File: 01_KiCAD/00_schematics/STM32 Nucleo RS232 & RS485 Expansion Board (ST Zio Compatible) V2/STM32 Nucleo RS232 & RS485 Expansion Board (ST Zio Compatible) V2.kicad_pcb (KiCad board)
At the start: 4 copper layers, 72 x 133.4 mm, 182 parts, among them CN10 Conn_02x17_Odd_Even, CN7 Conn_02x10_Odd_Even, CN8 Conn_02x08_Odd_Even, CN9 Conn_02x15_Odd_Even, IC1 REG103GA-A, J1 1190299, J10 DIR, J11 TERM_TX, J12 TERM_RX, J13 SLR, J14 HD-A(Y), J15 HD-B(Z), J2 CONN D-SUB PLUG 9POS TH, J3 TCVR_PWR, J4 TX_LED, J5 RX_LED, J6 SW_ENA, J7 MODE0, J8 MODE1, J9 MODE2, U1 TPS2117DRLR, U11 SN74LVC2G14DBV, U12 SN74LVC14ADR, U2 THVD4431RHAR, U3 SN74LVC2G14DBV, U4 SN74LVC245ADBR, U5 SN74LVC14ADR, U6 NUCLEO-H753ZI

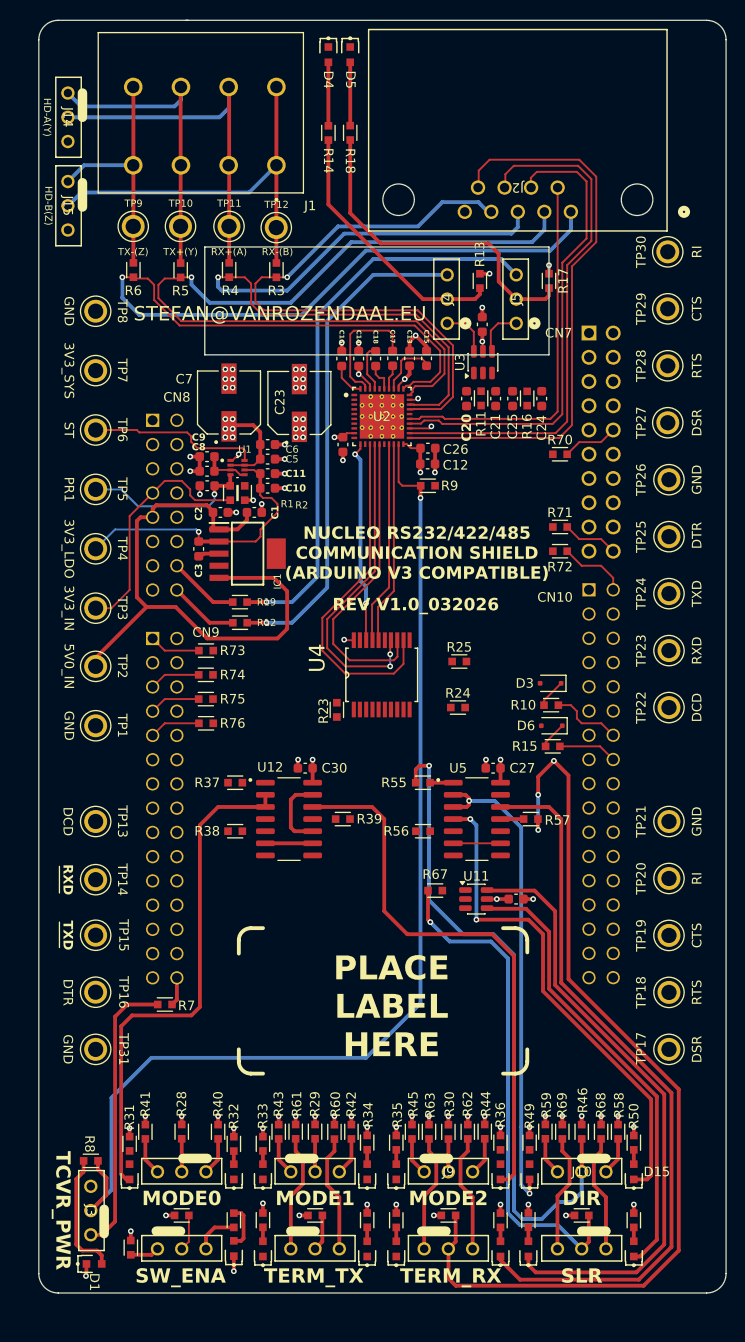
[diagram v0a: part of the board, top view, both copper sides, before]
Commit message: Finalizing roting
Made some final routings and updated Netlist name on the schematics for some of the RS232 testpoints.
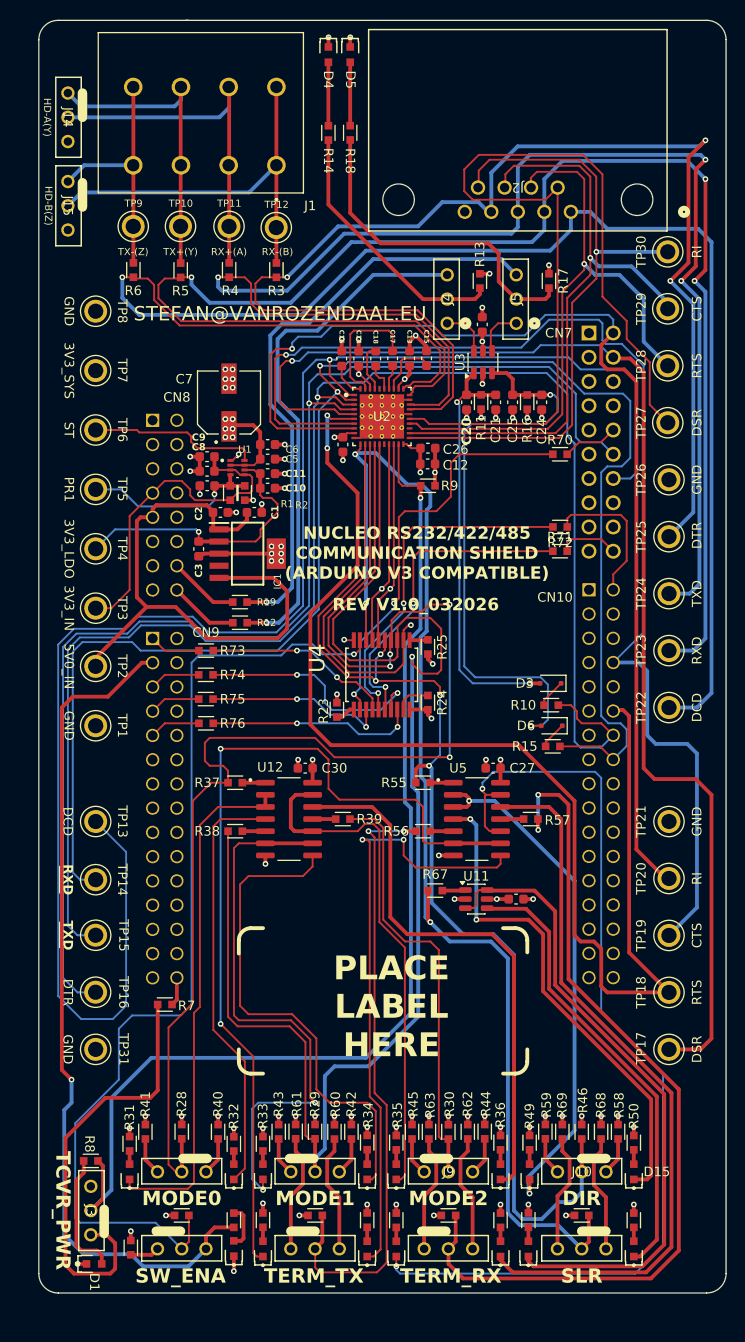
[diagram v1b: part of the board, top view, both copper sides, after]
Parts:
- removed C23: 47µF, EEEFT1H470AP:CAP_EEEFT1H470AP
- moved R25 3.63 mm to (68.6, 102.5), turned to -90 degrees
- moved R24 3.19 mm to (68.6, 108.3), turned to -90 degrees
- moved R72 2.54 mm to (82.4, 89.9)
- moved R71 2.54 mm to (82.4, 92.5)
- moved C20 0.38 mm to (72.6, 76.8)
- moved C21 0.38 mm to (75.7, 76.8)
- moved C24 0.38 mm to (80.5, 76.8)
- moved C25 0.38 mm to (77.5, 76.8)
- moved R11 0.38 mm to (74.2, 76.8)
- moved R16 0.38 mm to (79.0, 76.8)
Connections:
- TP27 pad TP: /RS232 & RS485 Tranceiver/DSR -> /RS232 & RS485 Tranceiver/DSRBus
- TP28 pad TP: /RS232 & RS485 Tranceiver/RTS -> /RS232 & RS485 Tranceiver/RTSBus
- TP29 pad TP: /RS232 & RS485 Tranceiver/CTS -> /RS232 & RS485 Tranceiver/CTSBus
- TP30 pad TP: /RS232 & RS485 Tranceiver/RI -> /RS232 & RS485 Tranceiver/RIBus
- U2 pad 42: (no net) -> GND
- U2 pad 43: (no net) -> GND
- U2 pad 44: (no net) -> GND
- U2 pad 45: (no net) -> GND
- U2 pad 46: (no net) -> GND
- U2 pad 47: (no net) -> GND
- U2 pad 48: (no net) -> GND
- U2 pad 49: (no net) -> GND
- U2 pad 50: (no net) -> GND
- U2 pad 51: (no net) -> GND
- U2 pad 52: (no net) -> GND
- U2 pad 53: (no net) -> GND
- U2 pad 54: (no net) -> GND
- U2 pad 55: (no net) -> GND
- U2 pad 56: (no net) -> GND
- U2 pad 57: (no net) -> GND
- U2 pad 58: (no net) -> GND
- U2 pad 59: (no net) -> GND
- U2 pad 60: (no net) -> GND
- U2 pad 61: (no net) -> GND
- U2 pad 62: (no net) -> GND
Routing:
- net L1-DCD: track 0.00 -> 173.1 mm, vias 0 -> 1
- net L2-RXD: track 6.16 -> 166.1 mm, vias 0 -> 2
- net L3-TXD: track 7.50 -> 165.3 mm, vias 0 -> 1
- net L4-DTR: track 0.00 -> 135.0 mm, vias 0 -> 1
- net L5-DSR: track 0.00 -> 132.4 mm, vias 0 -> 1
- net L6-RTS: track 0.00 -> 131.2 mm, vias 0 -> 2
- net L7-CTS: track 0.00 -> 127.5 mm, vias 0 -> 1
- net L8-RI: track 0.00 -> 118.6 mm, vias 0 -> 1
- net MODE1: track 35.7 -> 151.7 mm, vias 0 -> 1
- net MODE2: track 39.5 -> 145.1 mm, vias 0 -> 1
- net Net-(D18-K): track 0.00 -> 103.8 mm, vias 0 -> 2
- net MODE0: track 37.1 -> 139.7 mm, vias 2 -> 4
- net Net-(J6-Pin_2): track 3.82 -> 102.6 mm, vias 0 -> 1
- net TERM_TX: track 25.5 -> 120.1 mm, vias 0 -> 3
- net Net-(D16-K): track 4.95 -> 97.7 mm, vias 0 -> 2
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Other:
- outline, holes or cut-outs redrawn

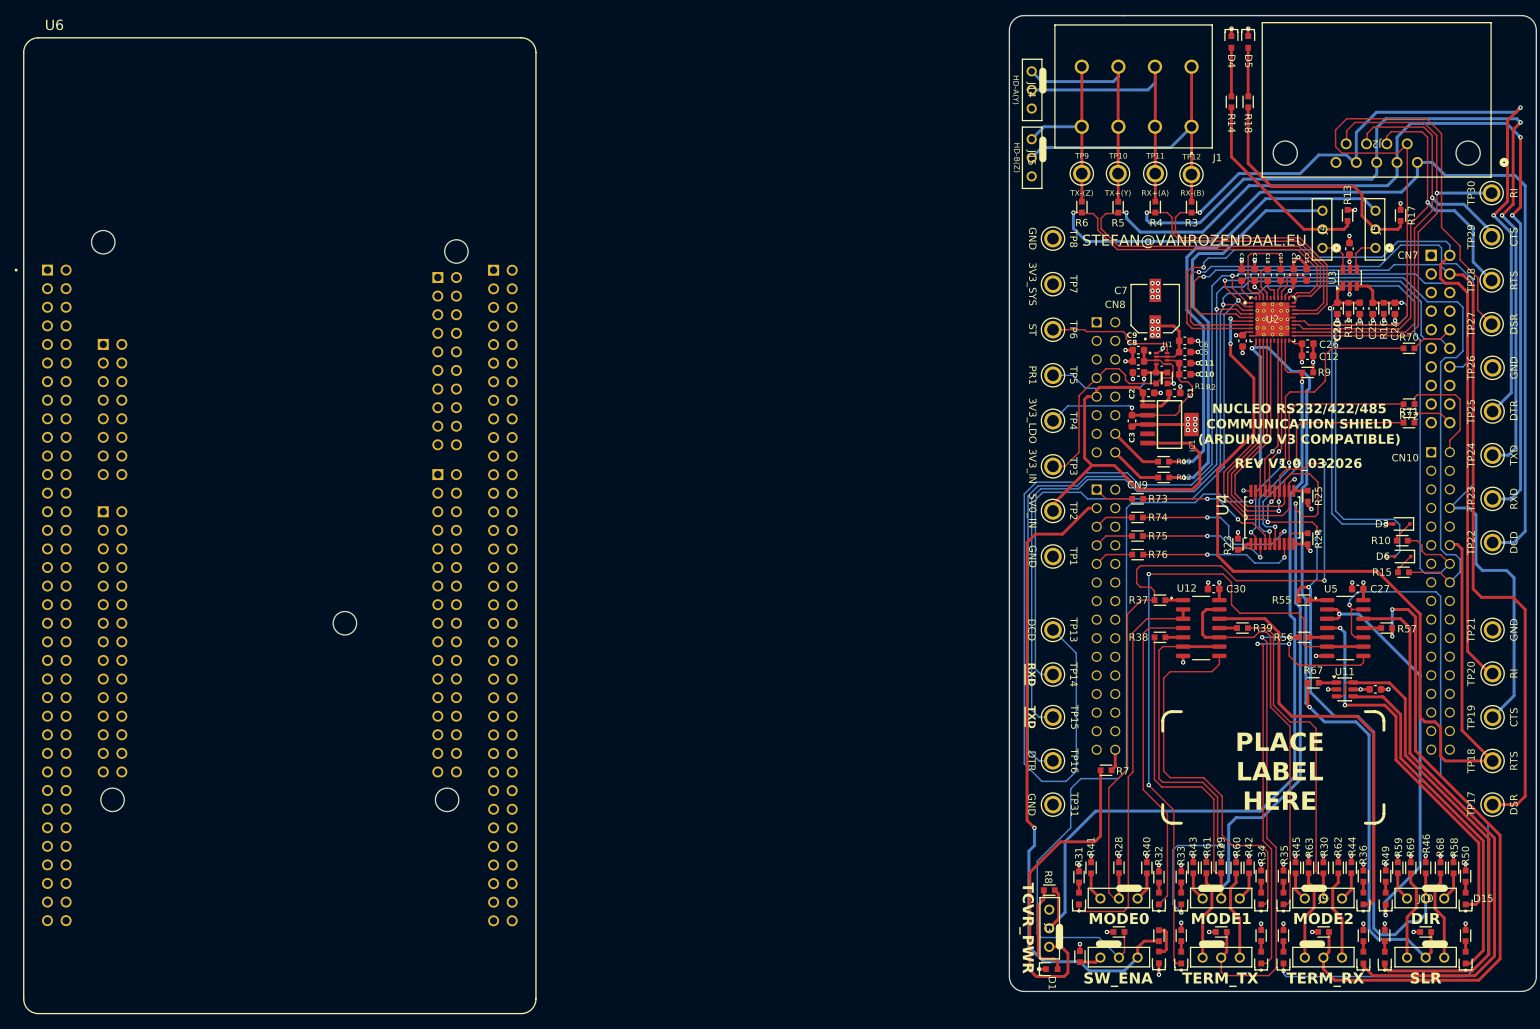
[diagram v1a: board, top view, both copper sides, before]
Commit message: Finalizing PCB Design
Finalizing track routing on PCB and run DRC. Made some minor silkscreen adjustments.
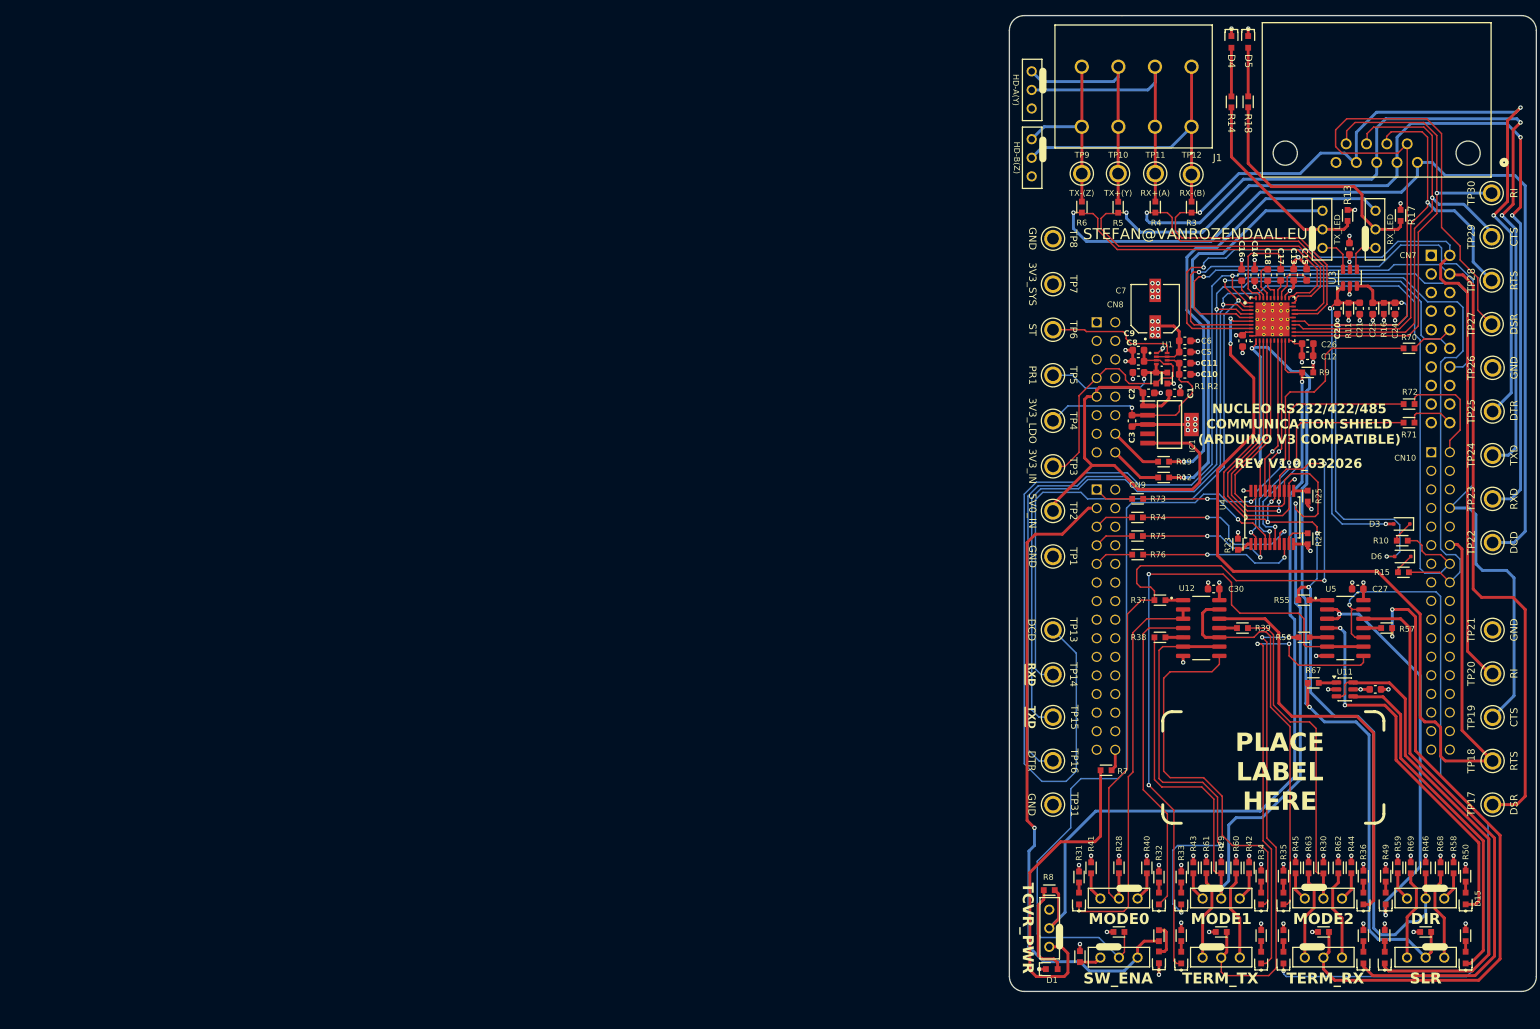
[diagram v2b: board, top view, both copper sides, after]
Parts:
- removed U6: NUCLEO-H753ZI, NUCLEO-H753ZI:MODULE_NUCLEO-H753ZI
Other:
- outline, holes or cut-outs redrawn
- rule pad_to_mask_clearance: 0.05 -> -0.05
- board text added: "≥8 MIL VIAS REQUIRE CONDUCTIVE FILL AND PLANARIZE"
- board text removed: "XX MIL VIAS REQUIRE CONDUCTIVE FILL AND PLANARIZE"

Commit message: Complete redesign
Redesigned the complete board. Added hardware termination jumpers for 1120R resistors for RS485. Changes footprint, package size and simplified values between capacitors.
Still need to re-route the entire board :-(
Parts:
- removed C33: 100nF, PCM_SparkFun-Capacitor:C_0603_1608Metric
- removed D21: LED, IN-S63AT:LED_0603_WRE
- removed IC1: REG103GA-A, REG103GA-A:SOT127P706X180-6N
- removed U11: SN74LVC2G14DBV, Package_TO_SOT_SMD:SOT-23-6
- removed U12: SN74LVC14ADR, SN74LVC14ADR:SOIC127P600X175-14N
- added C23: 470nF, PCM_SparkFun-Capacitor:C_0603_1608Metric, F.Cu at (-122.9, 80.4)
- added C28: 100nF, PCM_SparkFun-Capacitor:C_0603_1608Metric, F.Cu at (-123.1, 71.3)
- added C29: 100nF, PCM_SparkFun-Capacitor:C_0603_1608Metric, F.Cu at (-138.1, 44.4)
- added C31: 100nF, PCM_SparkFun-Capacitor:C_0603_1608Metric, F.Cu at (-20.8, 93.9)
- added D2: BAT54J, Diode_SMD:D_SOD-323F, F.Cu at (-20.2, 88.3)
- added J16: TERM_RX, Samtec_Connector:Samtec HTSW-103-07-F-S, F.Cu at (-144.9, 41.2)
- added J17: SLR, Samtec_Connector:Samtec HTSW-103-07-F-S, F.Cu at (-144.9, 47.6)
- added R20: 137R, PCM_fab:R_0603, F.Cu at (56.1, 39.7)
- added R21: 330R, PCM_fab:R_0603, F.Cu at (-138.2, 41.8)
- added U6: SN74LVC14ADR, SN74LVC14ADR:SOIC127P600X175-14N, F.Cu at (-116.4, 72.4)
- added U7: SN74LVC14ADR, SN74LVC14ADR:SOIC127P600X175-14N, F.Cu at (-8.72, 125.3)
- added U8: SN74LVC2G14DBV, Package_TO_SOT_SMD:SOT-23-6, F.Cu at (-120.8, 101.8)
- C1, C18, C19, C2, C21, C5: footprint PCM_SparkFun-Capacitor:C_0603_1608Metric -> Capacitor_SMD:C_0805_2012Metric
- C10: value 1µF -> 2µ2; footprint PCM_SparkFun-Capacitor:C_0603_1608Metric -> Capacitor_SMD:C_1210_3225Metric
- C11: value 100nF -> 47µF; footprint PCM_SparkFun-Capacitor:C_0603_1608Metric -> EEEFT1H470AP:CAP_EEEFT1H470AP
- C12: value 1µF -> 47µF; footprint PCM_SparkFun-Capacitor:C_0603_1608Metric -> EEEFT1H470AP:CAP_EEEFT1H470AP
- C13, C14: value 1µF -> 100nF
- C15, C16, C17: value 100nF -> 1µF; footprint PCM_SparkFun-Capacitor:C_0603_1608Metric -> Capacitor_SMD:C_1206_3216Metric
- C20: value 470nF -> 100nF; footprint PCM_SparkFun-Capacitor:C_0603_1608Metric -> Capacitor_SMD:C_0805_2012Metric
- C24: value 470nF -> 100nF
- C26: value 100nF -> 470nF
- C3: value 100nF -> 2µ2; footprint PCM_SparkFun-Capacitor:C_0603_1608Metric -> Capacitor_SMD:C_0805_2012Metric
- C4: value 10nF -> 1µ; footprint PCM_SparkFun-Capacitor:C_0603_1608Metric -> Capacitor_SMD:C_0805_2012Metric
- C6: value 470nF -> 1µ; footprint PCM_SparkFun-Capacitor:C_0603_1608Metric -> Capacitor_SMD:C_0805_2012Metric
- C7: value 47µF -> 100nF; footprint EEEFT1H470AP:CAP_EEEFT1H470AP -> Capacitor_SMD:C_0805_2012Metric
- C8: value 1µF -> 100nF; footprint PCM_SparkFun-Capacitor:C_0603_1608Metric -> Capacitor_SMD:C_0603_1608Metric
- C9: value 100nF -> 1µ; footprint PCM_SparkFun-Capacitor:C_0603_1608Metric -> Capacitor_SMD:C_0805_2012Metric
- D3, D6: value BAT54J -> LED; footprint Diode_SMD:D_SOD-323F -> IN-S63AT:LED_0603_WRE
- D5: value LED -> BAT54J; footprint IN-S63AT:LED_0603_WRE -> Diode_SMD:D_SOD-323F
- J1: value 1190299 -> HD-A(Y); footprint PH1190299:PHOENIX_1190299 -> Samtec_Connector:Samtec HTSW-103-07-F-S
- J10: value DIR -> SW_ENA
- J11: value TERM_TX -> MODE0
- J12: value TERM_RX -> MODE1
- J13: value SLR -> MODE2
- J14: value HD-A(Y) -> DIR
- J15: value HD-B(Z) -> TERM_TX
- J2: value CONN D-SUB PLUG 9POS TH -> HD-B(Z); footprint SubD-M-2301843-2:CONN9_2301843-2_TEC -> Samtec_Connector:Samtec HTSW-103-07-F-S
- J3: value TCVR_PWR -> TERM_RX (A/B)
- J4: value TX_LED -> TERM_TX (Y/Z)
- J5: value RX_LED -> 1190299; footprint Samtec_Connector:Samtec HTSW-103-07-F-S -> PH1190299:PHOENIX_1190299
- J6: value SW_ENA -> CONN D-SUB PLUG 9POS TH; footprint Samtec_Connector:Samtec HTSW-103-07-F-S -> SubD-M-2301843-2:CONN9_2301843-2_TEC
- J7: value MODE0 -> TCVR_PWR
- J8: value MODE1 -> TX_LED
- J9: value MODE2 -> RX_LED
- R10: value 1K -> 590R
- R11: value 453K -> 10K
- R12: value 330R -> 1K
- R13: value 1M -> 453K
- R14: value 590R -> 330R
- R15: value 1K -> 1M
- R16: value 453K -> 590R
- R17: value 1M -> 1K
- R18: value 137R -> 453K
- R19: value 330R -> 1M
- R3, R4: value 0R -> 120R
- R7: value 330R -> 0R
- R8: value 590R -> 0R
- R9: value 10K -> 330R
- TP10: value TX+(Y) -> DCD
- TP11: value RX+(A) -> TX-(Z); footprint 5008_Orange:KEYSTONE_5008 -> 5009_Yellow:KEYSTONE_5009
- TP12: value RX-(B) -> RXD; footprint 5008_Orange:KEYSTONE_5008 -> 5009_Yellow:KEYSTONE_5009
- TP13: value DCD -> RXD
- TP14: value RXD -> TX+(Y)
- TP16: value DTR -> TXD; footprint 5009_Yellow:KEYSTONE_5009 -> 5008_Orange:KEYSTONE_5008
- TP17: value DSR -> RX+(A); footprint 5009_Yellow:KEYSTONE_5009 -> 5008_Orange:KEYSTONE_5008
- TP18: value RTS -> DTR
- TP19: value CTS -> DTR; footprint 5009_Yellow:KEYSTONE_5009 -> 5008_Orange:KEYSTONE_5008
- TP20: value RI -> RX-(B); footprint 5009_Yellow:KEYSTONE_5009 -> 5008_Orange:KEYSTONE_5008
- TP21: value GND -> DSR; footprint 5006_Black:KEYSTONE_5006 -> 5009_Yellow:KEYSTONE_5009
- TP22: value DCD -> GND; footprint 5009_Yellow:KEYSTONE_5009 -> 5006_Black:KEYSTONE_5006
- TP23: value RXD -> RTS
- TP24: value TXD -> DSR
- TP25: value DTR -> CTS; footprint 5008_Orange:KEYSTONE_5008 -> 5009_Yellow:KEYSTONE_5009
- TP26: value GND -> RTS; footprint 5006_Black:KEYSTONE_5006 -> 5008_Orange:KEYSTONE_5008
- TP27: value DSR -> RI; footprint 5008_Orange:KEYSTONE_5008 -> 5009_Yellow:KEYSTONE_5009
- TP28: value RTS -> CTS
- TP29: value CTS -> GND; footprint 5008_Orange:KEYSTONE_5008 -> 5006_Black:KEYSTONE_5006
- TP3: value 3V3_IN -> 3V3_LDO
- TP4: value 3V3_LDO -> GND; footprint 5005_Red:KEYSTONE_5005 -> 5006_Black:KEYSTONE_5006
- TP5: value PR1 -> 3V3_IN
- TP6: value ST -> 3V3_SYS; footprint 5007_White:KEYSTONE_5007 -> 5005_Red:KEYSTONE_5005
- TP7: value 3V3_SYS -> PR1
- TP8: value GND -> ST; footprint 5006_Black:KEYSTONE_5006 -> 5005_Red:KEYSTONE_5005
- TP9: value TX-(Z) -> DCD
- U1: value TPS2117DRLR -> TLV77518PDBVR; footprint TPS2117DRLR:SOTFL50P160X60-8N -> TLV77518PDBVR:SOT-23-5_1P75X3P05_TEX
- U2: value THVD4431RHAR -> TPS2117DRLR; footprint THVD4431RHAR:RHA0040R-MFG -> TPS2117DRLR:SOTFL50P160X60-8N
- U3: value SN74LVC2G14DBV -> THVD4431RHAR; footprint Package_TO_SOT_SMD:SOT-23-6 -> THVD4431RHAR:RHA0040R-MFG
- U4: value SN74LVC245ADBR -> SN74LVC2G14DBV; footprint SN74LVC245ADBR:SOP65P780X200-20N -> Package_TO_SOT_SMD:SOT-23-6
- U5: value SN74LVC14ADR -> SN74LVC245ADBR; footprint SN74LVC14ADR:SOIC127P600X175-14N -> SN74LVC245ADBR:SOP65P780X200-20N
- moved U5 214.9 mm to (-139.8, 96.0), turned to 90 degrees
- moved C30 205.5 mm to (-138.1, 46.9), turned to 0 degrees
- moved R1 185.0 mm to (-135.9, 64.5)
- moved R19 166.6 mm to (-117.1, 83.6)
- moved R12 166.3 mm to (-116.8, 86.9)
- moved R2 162.4 mm to (-111.9, 67.4)
- moved J15 147.9 mm to (-115.3, 34.0)
- moved C22 138.6 mm to (-63.8, 56.8)
- moved D1 138.6 mm to (-104.4, 155.2)
- moved D10 138.6 mm to (-86.7, 145.5)
- moved D11 138.6 mm to (-75.8, 145.5)
- moved D12 138.6 mm to (-72.8, 145.5)
- moved D13 138.6 mm to (-61.8, 145.5)
- moved D14 138.6 mm to (-58.8, 145.5)
- moved D15 138.6 mm to (-47.9, 145.5)
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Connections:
- C10 pad 1: 3V3_LDO -> 3V3_SYS
- C11 pad 1: 3V3_LDO -> 3V3_SYS
- C13 pad 1: 3V3_SYS -> RX+ (A)
- C13 pad 2: GND -> Net-(J3-Pin_2)
- C14 pad 1: 3V3_SYS -> TX+ (Y)
- C14 pad 2: GND -> Net-(J4-Pin_2)
- C15 pad 1: Net-(U2-V-) -> 3V3_SYS
- C16 pad 1: Net-(U2-V+) -> 3V3_SYS
- C17 pad 1: Net-(U2-C2+) -> 3V3_SYS
- C17 pad 2: Net-(U2-C2-) -> GND
- C18 pad 1: Net-(U2-C1+) -> Net-(U3-V-)
- C18 pad 2: Net-(U2-C1-) -> GND
- C19 pad 1: 3V3_SYS -> Net-(U3-V+)
- C2 pad 1: ARDUINO_5V -> 3V3_LDO
- C20 pad 1: GND -> Net-(U3-C1-)
- C20 pad 2: /Rx & Tx LED/TX_RC -> Net-(U3-C2-)
- C21 pad 1: /Rx & Tx LED/TX_RC -> Net-(U3-C1+)
- C21 pad 2: GND -> Net-(U3-C2+)
- C24 pad 1: GND -> /Rx & Tx LED/TX_RC
- C24 pad 2: /Rx & Tx LED/RX_RC -> GND
- C25 pad 1: /Rx & Tx LED/RX_RC -> 3V3_SYS
- C26 pad 1: 3V3_SYS -> GND
- C26 pad 2: GND -> /Rx & Tx LED/RX_RC
- C27 pad 1: 3V3_SYS -> /Rx & Tx LED/RX_RC
- C4 pad 1: Net-(U1-PR1) -> NUCLEO_3V3
- C5 pad 1: 3V3_SYS -> NUCLEO_3V3
- C6 pad 1: GND -> 3V3_LDO
- C6 pad 2: 3V3_SYS -> GND
- C7 pad 1: 3V3_SYS -> 3V3_LDO
- C8 pad 1: NUCLEO_3V3 -> 3V3_SYS
- C9 pad 1: NUCLEO_3V3 -> 3V3_SYS
- D3 pad 1: Net-(D3-K) -> GND
- D3 pad 2: /Rx & Tx LED/TX_RC -> Net-(D3-A)
- D5 pad 1: GND -> Net-(D5-K)
- D5 pad 2: Net-(D5-A) -> /Rx & Tx LED/RX_RC
- D6 pad 1: Net-(D6-K) -> GND
- D6 pad 2: /Rx & Tx LED/RX_RC -> Net-(D6-A)
- D7 pad 1: GND -> Net-(D7-K)
- J10 pad 2: DIR -> Net-(J10-Pin_2)
- J10 pad 3: Net-(J10-Pin_3) -> MCU_OE
- J11 pad 2: TERM_TX -> MODE0
- J12 pad 2: TERM_RX -> MODE1
- J13 pad 2: SLR -> MODE2
- J14 pad 1: /RS232 & RS485 Tranceiver/TX+ (Y) -> Net-(J14-Pin_1)
- J14 pad 2: /RS232 & RS485 Tranceiver/RX+ (A) -> DIR
- J14 pad 3: unconnected-(J14-Pin_3-Pad3) -> Net-(J14-Pin_3)
- J15 pad 1: /RS232 & RS485 Tranceiver/TX- (Z) -> Net-(J15-Pin_1)
- J15 pad 2: /RS232 & RS485 Tranceiver/RX- (B) -> TERM_TX
- J15 pad 3: unconnected-(J15-Pin_3-Pad3) -> Net-(J15-Pin_3)
- J2 pad 1: /RS232 & RS485 Tranceiver/TX- -> unconnected-(J2-Pin_1-Pad1)
- J2 pad 2: /RS232 & RS485 Tranceiver/TX+ -> TX- (Z)
- J2 pad 3: /RS232 & RS485 Tranceiver/RX+ -> RX- (B)
- J3 pad 1: 3V3_SYS -> unconnected-(J3-Pin_1-Pad1)
- J3 pad 2: /RS232 & RS485 Tranceiver/THVD_SHDN_N -> Net-(J3-Pin_2)
- J3 pad 3: Net-(J3-Pin_3) -> RX- (B)
- J4 pad 1: /Rx & Tx LED/TX_ACT -> unconnected-(J4-Pin_1-Pad1)
- J4 pad 3: Net-(J4-Pin_3) -> TX- (Z)
- J6 pad 1: Net-(J6-Pin_1) -> /RS232 & RS485 Tranceiver/TX-
- J6 pad 2: Net-(J6-Pin_2) -> /RS232 & RS485 Tranceiver/TX+
- J6 pad 3: MCU_OE -> /RS232 & RS485 Tranceiver/RX+
- J7 pad 1: Net-(J7-Pin_1) -> 3V3_SYS
- J7 pad 2: MODE0 -> /RS232 & RS485 Tranceiver/THVD_SHDN_N
- J8 pad 1: Net-(J8-Pin_1) -> /Rx & Tx LED/TX_ACT
- J8 pad 2: MODE1 -> Net-(J8-Pin_2)
- J9 pad 1: Net-(J9-Pin_1) -> /Rx & Tx LED/RX_ACT
- J9 pad 2: MODE2 -> Net-(J9-Pin_2)
- R1 pad 2: Net-(U1-PR1) -> Net-(U2-PR1)
- R10 pad 1: L3-TXD -> /RS232 & RS485 Tranceiver/THVD_SHDN_N
- R10 pad 2: Net-(D3-K) -> Net-(D1-A)
- R11 pad 1: 3V3_SYS -> /RS232 & RS485 Tranceiver/THVD_SHDN_N
- R11 pad 2: /Rx & Tx LED/TX_RC -> GND
- R12 pad 1: MCU_TXLED_GPIO -> L3-TXD
- R12 pad 2: Net-(J4-Pin_3) -> Net-(D2-K)
- R13 pad 1: Net-(J4-Pin_2) -> 3V3_SYS
- R13 pad 2: GND -> /Rx & Tx LED/TX_RC
- R14 pad 1: Net-(J4-Pin_2) -> MCU_TXLED_GPIO
- R14 pad 2: Net-(D4-A) -> Net-(J8-Pin_3)
- R15 pad 1: L2-RXD -> Net-(J8-Pin_2)
- R15 pad 2: Net-(D6-K) -> GND
- R16 pad 1: 3V3_SYS -> Net-(J8-Pin_2)
- R16 pad 2: /Rx & Tx LED/RX_RC -> Net-(D3-A)
- R17 pad 1: GND -> L2-RXD
- R17 pad 2: Net-(J5-Pin_2) -> Net-(D5-K)
- R18 pad 1: Net-(D5-A) -> 3V3_SYS
- R18 pad 2: Net-(J5-Pin_2) -> /Rx & Tx LED/RX_RC
- R19 pad 1: MCU_RXLED_GPIO -> GND
- R19 pad 2: Net-(J5-Pin_3) -> Net-(J9-Pin_2)
- R2 pad 1: Net-(U1-PR1) -> Net-(U2-PR1)
- R22 pad 2: Net-(J6-Pin_1) -> Net-(J10-Pin_1)
- R23 pad 2: Net-(U4-DIR) -> Net-(U5-DIR)
- R24 pad 1: Net-(U4-A8) -> Net-(U5-A8)
- R25 pad 1: Net-(U4-B8) -> Net-(U5-B8)
- R26 pad 2: Net-(D7-A) -> Net-(D6-A)
- R27 pad 1: Net-(J6-Pin_2) -> Net-(J10-Pin_2)
- R3 pad 1: /RS232 & RS485 Tranceiver/RX- (B) -> RX+ (A)
- R3 pad 2: /RS232 & RS485 Tranceiver/RX- -> Net-(J3-Pin_2)
- R31 pad 1: Net-(D8-A) -> Net-(D7-A)
- R32 pad 2: Net-(D9-A) -> Net-(D8-A)
- R33 pad 1: Net-(D10-A) -> Net-(D9-A)
- R34 pad 2: Net-(D11-A) -> Net-(D10-A)
- R35 pad 1: Net-(D12-A) -> Net-(D11-A)
- R36 pad 2: Net-(D13-A) -> Net-(D12-A)
- R4 pad 1: /RS232 & RS485 Tranceiver/RX+ (A) -> TX+ (Y)
- R4 pad 2: /RS232 & RS485 Tranceiver/RX+ -> Net-(J4-Pin_2)
- R40 pad 2: Net-(J7-Pin_3) -> Net-(J11-Pin_3)
- R41 pad 2: Net-(J7-Pin_1) -> Net-(J11-Pin_1)
- R42 pad 2: Net-(J8-Pin_3) -> Net-(J12-Pin_3)
- R43 pad 2: Net-(J8-Pin_1) -> Net-(J12-Pin_1)
- R44 pad 2: Net-(J9-Pin_3) -> Net-(J13-Pin_3)
- R45 pad 2: Net-(J9-Pin_1) -> Net-(J13-Pin_1)
- R49 pad 1: Net-(D14-A) -> Net-(D13-A)
- R5 pad 1: /RS232 & RS485 Tranceiver/TX+ (Y) -> RX- (B)
- R5 pad 2: /RS232 & RS485 Tranceiver/TX+ -> /RS232 & RS485 Tranceiver/RX-
- R50 pad 2: Net-(D15-A) -> Net-(D14-A)
- R51 pad 1: Net-(D16-A) -> Net-(D15-A)
- R52 pad 2: Net-(D17-A) -> Net-(D16-A)
- R53 pad 1: Net-(D18-A) -> Net-(D17-A)
- R54 pad 2: Net-(D19-A) -> Net-(D18-A)
- R55 pad 2: Net-(U5A-1A) -> Net-(U7A-1A)
- R56 pad 2: Net-(U5C-3A) -> Net-(U7C-3A)
- R57 pad 2: Net-(U5E-5A) -> Net-(U7E-5A)
- R58 pad 2: Net-(J10-Pin_3) -> Net-(J14-Pin_3)
- R59 pad 2: Net-(J10-Pin_1) -> Net-(J14-Pin_1)
- R6 pad 1: /RS232 & RS485 Tranceiver/TX- (Z) -> RX+ (A)
- R6 pad 2: /RS232 & RS485 Tranceiver/TX- -> /RS232 & RS485 Tranceiver/RX+
- R60 pad 2: Net-(J11-Pin_3) -> Net-(J15-Pin_3)
- R61 pad 2: Net-(J11-Pin_1) -> Net-(J15-Pin_1)
- R62 pad 2: Net-(J12-Pin_3) -> Net-(J16-Pin_3)
- R63 pad 2: Net-(J12-Pin_1) -> Net-(J16-Pin_1)
- R65 pad 1: Net-(D20-A) -> Net-(D19-A)
- R66 pad 2: Net-(D21-A) -> Net-(D20-A)
- R68 pad 2: Net-(J13-Pin_3) -> Net-(J17-Pin_3)
- R69 pad 2: Net-(J13-Pin_1) -> Net-(J17-Pin_1)
- R7 pad 1: Net-(J3-Pin_3) -> TX+ (Y)
- R7 pad 2: MCU_SHDN -> /RS232 & RS485 Tranceiver/TX+
- R8 pad 1: /RS232 & RS485 Tranceiver/THVD_SHDN_N -> TX- (Z)
- R8 pad 2: Net-(D1-A) -> /RS232 & RS485 Tranceiver/TX-
- R9 pad 1: /RS232 & RS485 Tranceiver/THVD_SHDN_N -> Net-(J7-Pin_3)
- R9 pad 2: GND -> MCU_SHDN
- TP10 pad TP: /RS232 & RS485 Tranceiver/TX+ (Y) -> /RS232 & RS485 Tranceiver/TX-
- TP11 pad TP: /RS232 & RS485 Tranceiver/RX+ (A) -> TX- (Z)
- TP12 pad TP: /RS232 & RS485 Tranceiver/RX- (B) -> L2-RXD
- TP13 pad TP: L1-DCD -> /RS232 & RS485 Tranceiver/TX+
- TP14 pad TP: L2-RXD -> TX+ (Y)
- TP16 pad TP: L4-DTR -> /RS232 & RS485 Tranceiver/RX+
- TP17 pad TP: L5-DSR -> RX+ (A)
- TP18 pad TP: L6-RTS -> L4-DTR
- TP19 pad TP: L7-CTS -> /RS232 & RS485 Tranceiver/RX-
- TP20 pad TP: L8-RI -> RX- (B)
- TP21 pad TP: GND -> L5-DSR
- TP22 pad TP: /RS232 & RS485 Tranceiver/TX- -> GND
- TP23 pad TP: /RS232 & RS485 Tranceiver/TX+ -> L6-RTS
- TP24 pad TP: /RS232 & RS485 Tranceiver/RX+ -> /RS232 & RS485 Tranceiver/DSRBus
- TP25 pad TP: /RS232 & RS485 Tranceiver/RX- -> L7-CTS
- TP26 pad TP: GND -> /RS232 & RS485 Tranceiver/RTSBus
- TP27 pad TP: /RS232 & RS485 Tranceiver/DSRBus -> L8-RI
- TP28 pad TP: /RS232 & RS485 Tranceiver/RTSBus -> /RS232 & RS485 Tranceiver/CTSBus
- TP29 pad TP: /RS232 & RS485 Tranceiver/CTSBus -> GND
- TP3 pad TP: NUCLEO_3V3 -> 3V3_LDO
- TP4 pad TP: 3V3_LDO -> GND
- TP5 pad TP: Net-(U1-PR1) -> NUCLEO_3V3
- TP6 pad TP: Net-(U1-ST) -> 3V3_SYS
- TP7 pad TP: 3V3_SYS -> Net-(U2-PR1)
- TP8 pad TP: GND -> Net-(U2-ST)
- TP9 pad TP: /RS232 & RS485 Tranceiver/TX- (Z) -> L1-DCD
- U1 pad 1: GND -> ARDUINO_5V
- U1 pad 2: 3V3_SYS -> GND
- U1 pad 3: NUCLEO_3V3 -> ARDUINO_5V
- U1 pad 4: Net-(U1-PR1) -> unconnected-(U1-NC-Pad4)
- U1 pad 5: NUCLEO_3V3 -> 3V3_LDO
- U2 pad 1: L1-DCD -> GND
- U2 pad 2: L2-RXD -> 3V3_SYS
- U2 pad 3: L3-TXD -> NUCLEO_3V3
- U2 pad 4: L4-DTR -> Net-(U2-PR1)
- U2 pad 5: L5-DSR -> NUCLEO_3V3
- U2 pad 6: L6-RTS -> 3V3_LDO
- U2 pad 7: L7-CTS -> 3V3_SYS
- U2 pad 8: L8-RI -> Net-(U2-ST)
- U3 pad 1: /Rx & Tx LED/TX_RC -> L1-DCD
- U3 pad 2: GND -> L2-RXD
- U3 pad 3: /Rx & Tx LED/RX_RC -> L3-TXD
- U3 pad 4: /Rx & Tx LED/RX_ACT -> L4-DTR
- U3 pad 5: 3V3_SYS -> L5-DSR
- U3 pad 6: /Rx & Tx LED/TX_ACT -> L6-RTS
- U4 pad 1: Net-(U4-DIR) -> /Rx & Tx LED/TX_RC
- U4 pad 2: MCU_SLR -> GND
- U4 pad 3: MCU_TERM_TX -> /Rx & Tx LED/RX_RC
- U4 pad 4: MCU_TERM_RX -> /Rx & Tx LED/RX_ACT
- U4 pad 5: MCU_DIR -> 3V3_SYS
- U4 pad 6: MCU_MODE0 -> /Rx & Tx LED/TX_ACT
- U5 pad 1: Net-(U5A-1A) -> Net-(U5-DIR)
- U5 pad 10: Net-(D18-K) -> GND
- U5 pad 11: Net-(U5E-5A) -> Net-(U5-B8)
- U5 pad 12: Net-(D19-K) -> MODE2
- U5 pad 13: Net-(D18-K) -> MODE1
- U5 pad 14: 3V3_SYS -> MODE0
- U5 pad 2: Net-(D14-K) -> MCU_SLR
- U5 pad 3: Net-(D14-K) -> MCU_TERM_TX
- U5 pad 4: Net-(D15-K) -> MCU_TERM_RX
- U5 pad 5: Net-(U5C-3A) -> MCU_DIR
- U5 pad 6: Net-(D16-K) -> MCU_MODE0
- U5 pad 7: GND -> MCU_MODE1
- U5 pad 8: Net-(D17-K) -> MCU_MODE2
- U5 pad 9: Net-(D16-K) -> Net-(U5-A8)
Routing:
- net L1-DCD: track 173.1 -> 0.00 mm, vias 1 -> 0
- net L2-RXD: track 166.1 -> 0.00 mm, vias 2 -> 0
- net L3-TXD: track 165.3 -> 0.00 mm, vias 1 -> 0
- net MODE1: track 151.7 -> 0.00 mm, vias 1 -> 0
- net TERM_RX: track 147.0 -> 0.00 mm, vias 3 -> 0
- net MODE2: track 145.1 -> 0.00 mm, vias 1 -> 0
- net MODE0: track 139.7 -> 0.00 mm, vias 4 -> 0
- net L4-DTR: track 135.0 -> 0.00 mm, vias 1 -> 0
- net L5-DSR: track 132.4 -> 0.00 mm, vias 1 -> 0
- net L6-RTS: track 131.2 -> 0.00 mm, vias 2 -> 0
- net SLR: track 129.6 -> 0.00 mm, vias 3 -> 0
- net L7-CTS: track 127.5 -> 0.00 mm, vias 1 -> 0
- net DIR: track 120.5 -> 0.00 mm, vias 4 -> 0
- net TERM_TX: track 120.1 -> 0.00 mm, vias 3 -> 0
- net L8-RI: track 118.6 -> 0.00 mm, vias 1 -> 0
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
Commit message: Updating routing
Update routing tracks and placing and re-ordering components on the board.
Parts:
- C1, C3, C4, C6, C9: footprint Capacitor_SMD:C_0805_2012Metric -> Capacitor_SMD:C_1206_3216Metric
- C10: footprint Capacitor_SMD:C_1210_3225Metric -> Capacitor_SMD:C_1206_3216Metric
- C8: footprint Capacitor_SMD:C_0603_1608Metric -> Capacitor_SMD:C_0805_2012Metric
- J3: value TERM_RX (A/B) -> TERM (A/B)
- J4: value TERM_TX (Y/Z) -> TERM (Y/Z)
- TP10, TP13: footprint 5009_Yellow:KEYSTONE_5009 -> 5122_Blue:KEYSTONE_5122
- TP12, TP15, TP18, TP21, TP23, TP25, TP27, TP9: footprint 5009_Yellow:KEYSTONE_5009 -> 5121_Green:KEYSTONE_5121
- TP16, TP19, TP24, TP26, TP28, TP30: footprint 5008_Orange:KEYSTONE_5008 -> 5122_Blue:KEYSTONE_5122
- moved J17 266.8 mm to (86.9, 179.7)
- moved J16 238.1 mm to (48.5, 180.0)
- moved J14 232.9 mm to (75.4, 179.6), turned to 0 degrees
- moved J15 227.5 mm to (59.3, 179.8), turned to 0 degrees
- moved U5 215.1 mm to (75.3, 97.8)
- moved R12 200.2 mm to (81.8, 111.9), turned to 180 degrees
- moved U6 191.7 mm to (66.7, 129.0)
- moved R21 190.3 mm to (45.0, 93.2), turned to 90 degrees
- moved C23 188.5 mm to (63.4, 51.8), turned to 180 degrees
- moved R1 182.9 mm to (46.3, 80.4), turned to 0 degrees
- moved D5 182.0 mm to (81.8, 116.2), turned to 0 degrees
- moved R19 176.9 mm to (54.5, 40.5), turned to 90 degrees
- moved TP27 166.9 mm to (95.5, 158.2)
- moved TP9 163.7 mm to (33.4, 140.8)
- moved R2 158.9 mm to (46.3, 82.0), turned to 180 degrees
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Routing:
- net /RS232 & RS485 Tranceiver/THVD_SHDN_N: track 0.00 -> 162.0 mm
- net /RS232 & RS485 Tranceiver/TX-: track 57.5 -> 143.6 mm, vias 0 -> 1
- net RX+ (A): track 41.0 -> 124.6 mm, vias 0 -> 1
- net /RS232 & RS485 Tranceiver/TX+: track 57.8 -> 132.5 mm, vias 0 -> 1
- net TX- (Z): track 23.1 -> 97.4 mm
- net /RS232 & RS485 Tranceiver/RX+: track 49.6 -> 114.2 mm, vias 0 -> 1
- net L1-DCD: track 0.00 -> 64.4 mm, vias 0 -> 1
- net Net-(J9-Pin_3): track 0.00 -> 63.6 mm, vias 0 -> 1
- net Net-(J8-Pin_3): track 0.00 -> 57.8 mm, vias 0 -> 1
- net L4-DTR: track 0.00 -> 56.9 mm, vias 0 -> 1
- net /RS232 & RS485 Tranceiver/RX-: track 50.6 -> 105.8 mm, vias 0 -> 1
- net L2-RXD: track 0.00 -> 52.4 mm, vias 0 -> 1
- net L3-TXD: track 0.00 -> 49.2 mm, vias 0 -> 1
- net L5-DSR: track 0.00 -> 45.0 mm, vias 0 -> 1
- net L6-RTS: track 0.00 -> 37.9 mm, vias 0 -> 1
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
